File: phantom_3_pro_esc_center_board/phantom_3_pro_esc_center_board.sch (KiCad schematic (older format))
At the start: 0 parts

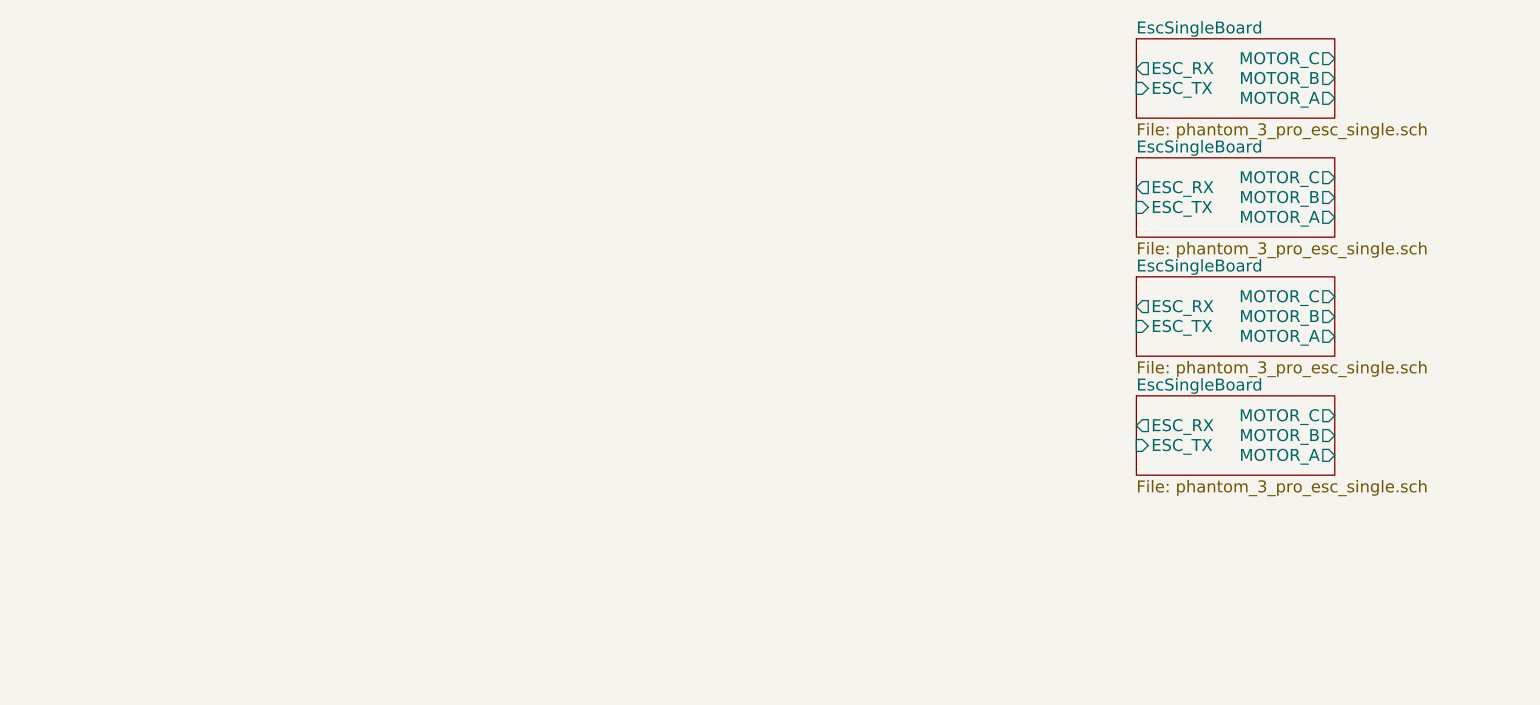
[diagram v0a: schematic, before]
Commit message: Renumbered components.
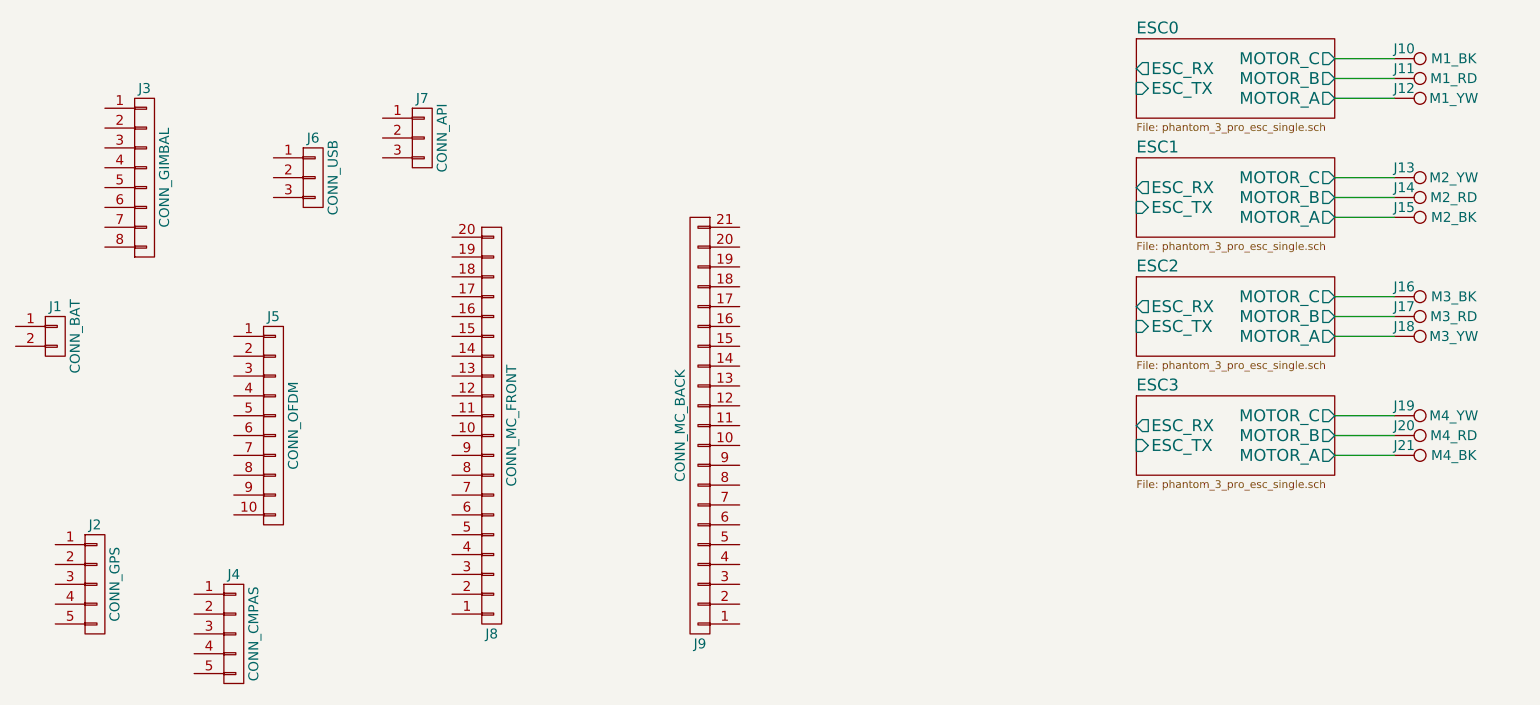
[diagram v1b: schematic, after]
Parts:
- added J1: CONN_BAT, symbol CONN_01X02
- added J10: M1_BK, symbol TEST_1P
- added J11: M1_RD, symbol TEST_1P
- added J12: M1_YW, symbol TEST_1P
- added J13: M2_YW, symbol TEST_1P
- added J14: M2_RD, symbol TEST_1P
- added J15: M2_BK, symbol TEST_1P
- added J16: M3_BK, symbol TEST_1P
- added J17: M3_RD, symbol TEST_1P
- added J18: M3_YW, symbol TEST_1P
- added J19: M4_YW, symbol TEST_1P
- added J2: CONN_GPS, symbol CONN_01X05
- added J20: M4_RD, symbol TEST_1P
- added J21: M4_BK, symbol TEST_1P
- added J3: CONN_GIMBAL, symbol CONN_01X08
- added J4: CONN_CMPAS, symbol CONN_01X05
- added J5: CONN_OFDM, symbol CONN_01X10
- added J6: CONN_USB, symbol CONN_01X03
- added J7: CONN_API, symbol CONN_01X03
- added J8: CONN_MC_FRONT, symbol CONN_01X20
- added J9: CONN_MC_BACK, symbol CONN_01X21
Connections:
- new net ESC0/MOTOR_A: J12.1
- new net ESC0/MOTOR_B: J11.1
- new net ESC0/MOTOR_C: J10.1
- new net ESC1/MOTOR_A: J15.1
- new net ESC1/MOTOR_B: J14.1
- new net ESC1/MOTOR_C: J13.1
- new net ESC2/MOTOR_A: J18.1
- new net ESC2/MOTOR_B: J17.1
- new net ESC2/MOTOR_C: J16.1
- new net ESC3/MOTOR_A: J21.1
- new net ESC3/MOTOR_B: J20.1
- new net ESC3/MOTOR_C: J19.1

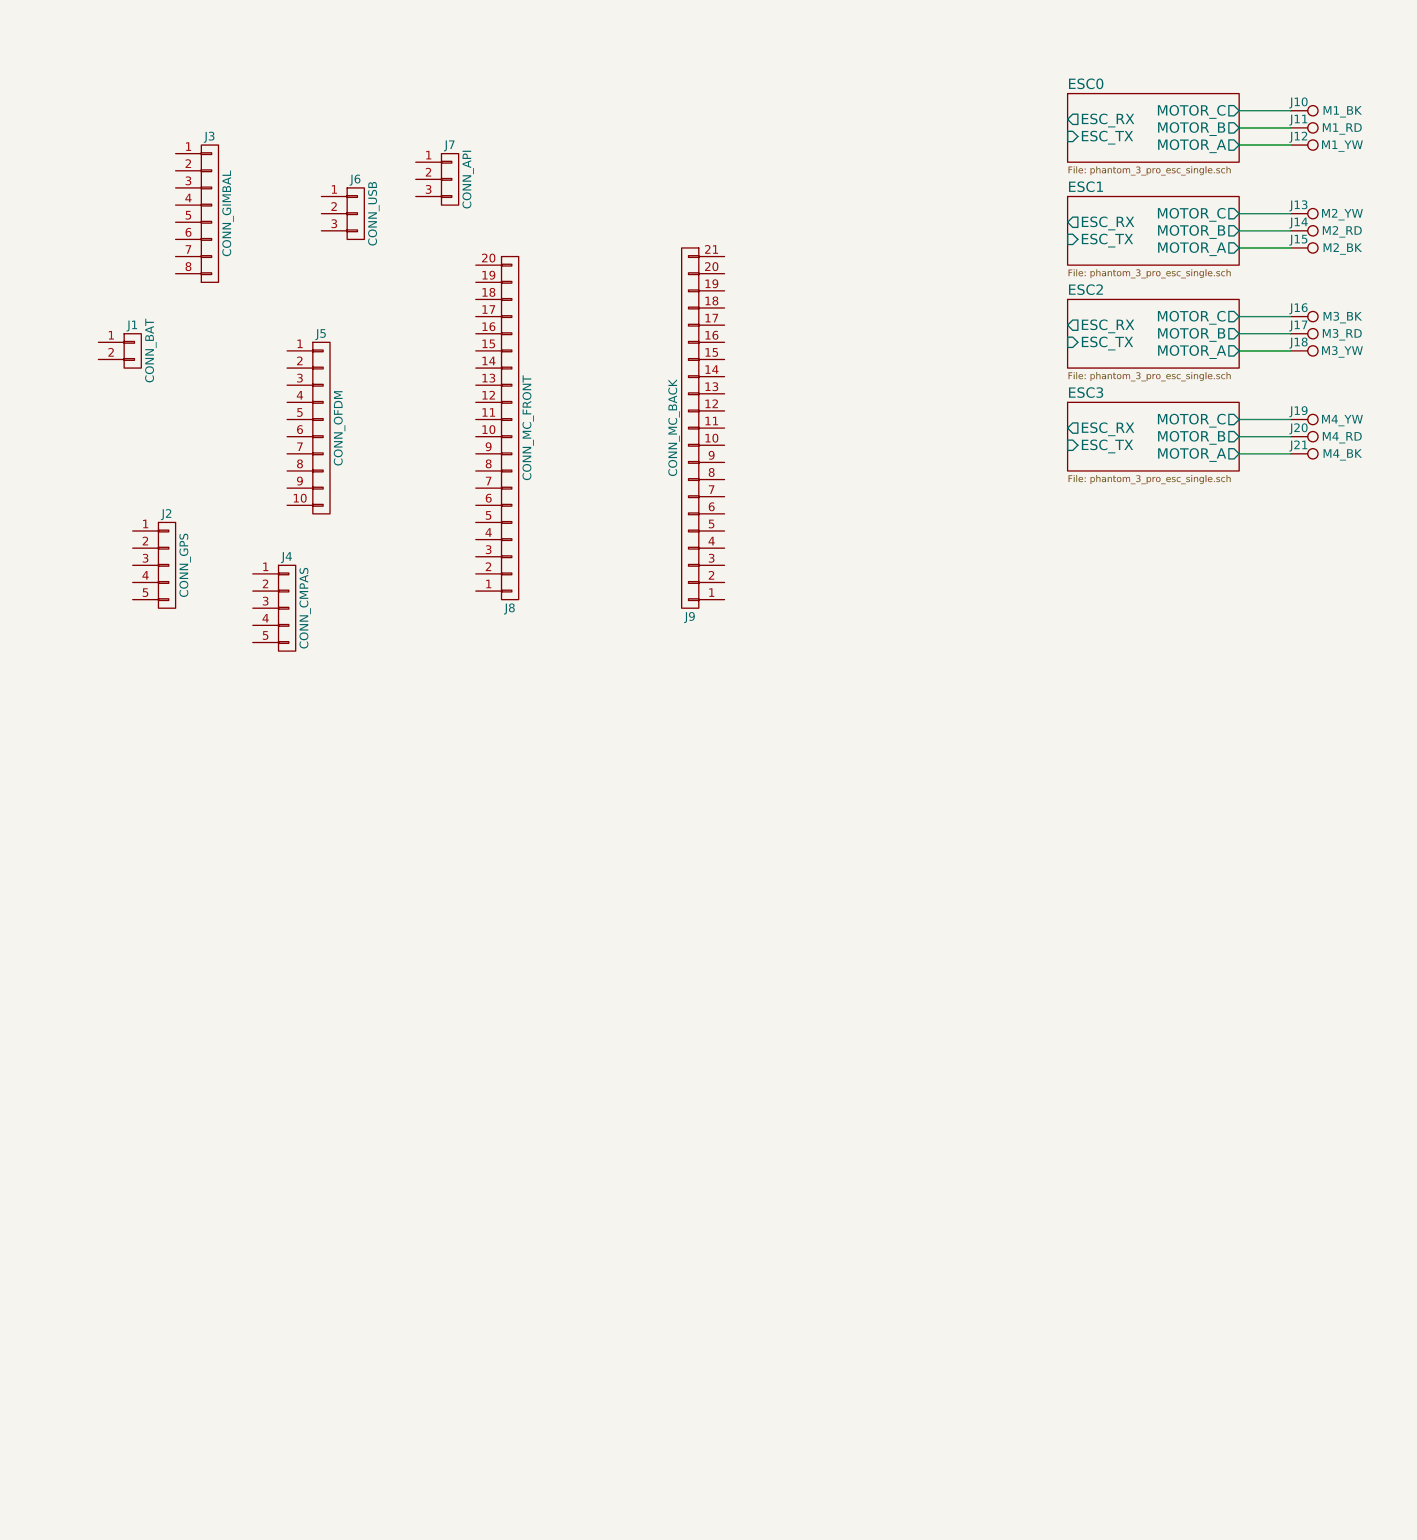
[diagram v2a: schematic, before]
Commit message: ESC Center: Identified pins of FC connection.
Named all FC pins, and linked with proper connectors.
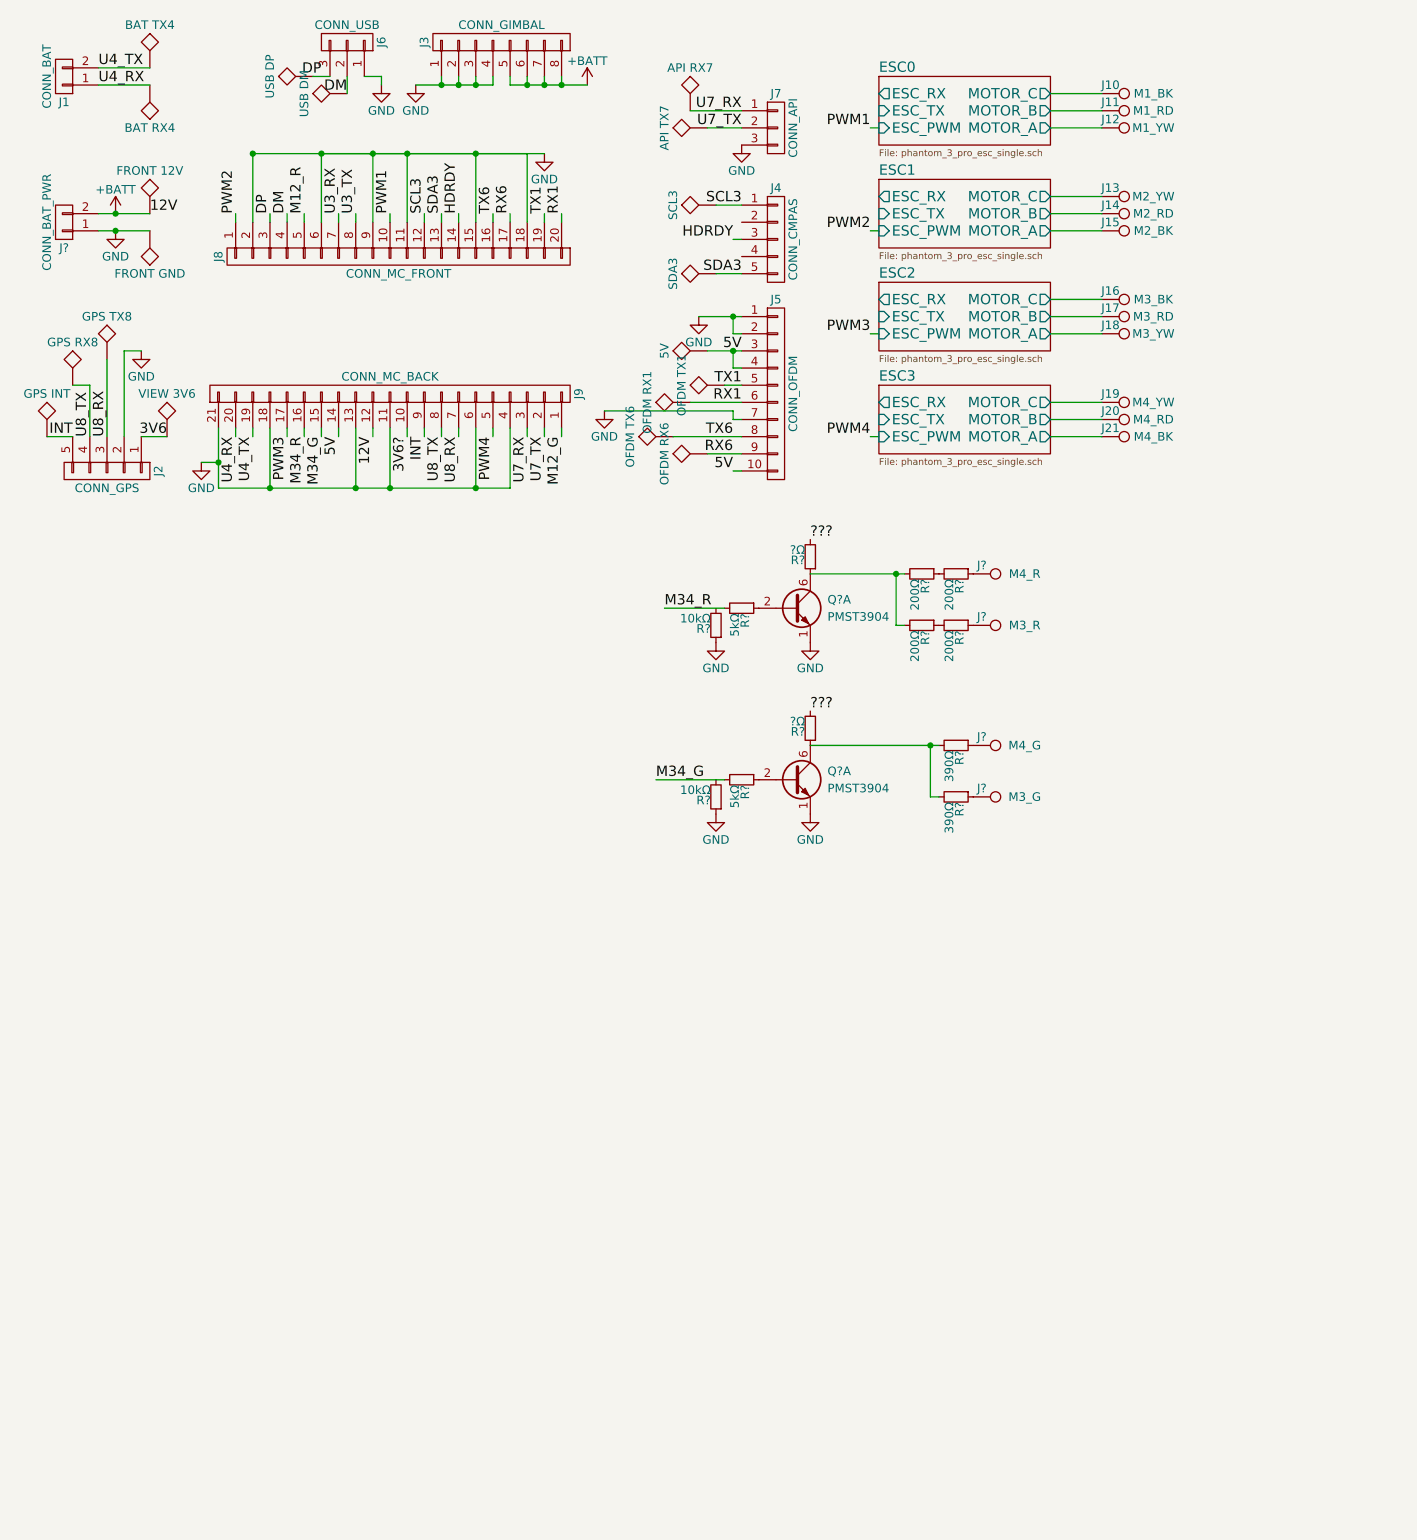
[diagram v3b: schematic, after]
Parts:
- added J?: CONN_BAT_PWR, symbol CONN_01X02
- added J?: M4_R, symbol TEST_1P
- added J?: M4_G, symbol TEST_1P
- added J?: M3_R, symbol TEST_1P
- added J?: M3_G, symbol TEST_1P
- added Q? (x2): PMST3904, TO_SOT_Packages_SMD:SOT-363, symbol PMBT2222AYS
- added R? (x4): 200Ω, symbol R_Small
- added R? (x2): 390Ω, symbol R_Small
- added R? (x2): 5kΩ, symbol R_Small
- added R? (x2): 10kΩ, symbol R_Small
- added R? (x2): ?Ω, symbol R_Small
- added TP?: GPS INT, symbol TEST
- added TP?: OFDM TX6, symbol TEST
- added TP?: GPS TX8, symbol TEST
- added TP?: FRONT 12V, symbol TEST
- added TP?: FRONT GND, symbol TEST
- added TP?: BAT TX4, symbol TEST
- added TP?: BAT RX4, symbol TEST
- added TP?: VIEW 3V6, symbol TEST
- added TP?: USB DP, symbol TEST
- added TP?: USB DM, symbol TEST
- added TP?: API RX7, symbol TEST
- added TP?: OFDM RX1, symbol TEST
- added TP?: API TX7, symbol TEST
- added TP?: 5V, symbol TEST
- added TP?: OFDM RX6, symbol TEST
- added TP?: SCL3, symbol TEST
- added TP?: SDA3, symbol TEST
- added TP?: OFDM TX1, symbol TEST
- added TP?: GPS RX8, symbol TEST
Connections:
- net PWM2: now reaches J8.1 (P1)
- net PWM1: now reaches J8.10 (P10)
- net GND: now reaches J8.11 (P11)
- net GND: now also J2.2 (P2), J3.1 (P1), J3.2 (P2), J3.3 (P3), J3.4 (P4), J5.1 (P1), J5.2 (P2), J5.7 (P7), J6.1 (P1), J7.3 (P3), J8.15 (P15), J8.18 (P18), J8.2 (P2), J8.6 (P6), J8.9 (P9), J9.11 (P11), J9.13 (P13), J9.18 (P18), J9.21 (P21), J9.4 (P4), J9.6 (P6), J?.1 (P1), Q?.1 (E1), Q?.1 (E1), R?.1, R?.1, TP?.1
- net SCL3: now reaches J8.12 (P12)
- net SCL3: now also J4.1 (P1), TP?.1
- net SDA3: now reaches J8.13 (P13)
- net SDA3: now also J4.5 (P5), TP?.1
- net HDRDY: now reaches J8.14 (P14)
- net HDRDY: now also J4.3 (P3)
- net TX6: now reaches J8.16 (P16)
- net TX6: now also J5.8 (P8), TP?.1
- net RX6: now reaches J8.17 (P17)
- net RX6: now also J5.9 (P9), TP?.1
- net TX1: now reaches J8.19 (P19)
- net TX1: now also J5.5 (P5), TP?.1
- net RX1: now reaches J8.20 (P20)
- net RX1: now also J5.6 (P6), TP?.1
- net DP: now reaches J8.3 (P3)
- net DP: now also J6.3 (P3), TP?.1
- net DM: now reaches J8.4 (P4)
- net DM: now also J6.2 (P2), TP?.1
- net M12_R: now reaches J8.5 (P5)
- net U3_RX: now reaches J8.7 (P7)
- net U3_TX: now reaches J8.8 (P8)
- net M12_G: now reaches J9.1 (P1)
- net 3V6?: now reaches J9.10 (P10)
- net +BATT: now reaches J9.12 (P12)
- net +BATT: now also J3.5 (P5), J3.6 (P6), J3.7 (P7), J3.8 (P8), J?.2 (P2), TP?.1
- net 5V: now reaches J9.14 (P14)
- net 5V: now also J5.10 (P10), J5.3 (P3), J5.4 (P4), TP?.1
- net M34_G: now reaches J9.15 (P15)
- net M34_G: now also R?.2
- net M34_R: now reaches J9.16 (P16)
- net M34_R: now also R?.2
- net PWM3: now reaches J9.17 (P17)
- net U4_TX: now reaches J9.19 (P19)
- net U4_TX: now also J1.2 (P2), TP?.1
- net U7_TX: now reaches J9.2 (P2)
- net U7_TX: now also J7.2 (P2), TP?.1
- net U4_RX: now reaches J9.20 (P20)
- net U4_RX: now also J1.1 (P1), TP?.1
- net U7_RX: now reaches J9.3 (P3)
- net U7_RX: now also J7.1 (P1), TP?.1
- net PWM4: now reaches J9.5 (P5)
- net U8_RX: now reaches J9.7 (P7)
- net U8_RX: now also J2.3 (P3), TP?.1
- net U8_TX: now reaches J9.8 (P8)
- net U8_TX: now also J2.4 (P4), TP?.1
- net INT: now reaches J9.9 (P9)
- net INT: now also J2.5 (P5), TP?.1
- net 3V6: now reaches J2.1 (P1)
- net 3V6: now also TP?.1
- new net: R?.1, R?.2 (x2)
- new net: Q?.6 (C1), R?.1, R?.2, R?.2 (x2)
- new net: J?.1, R?.1 (x4)
- new net: Q?.2 (B1), R?.1 (x2)
- new net ???: R?.2, R?.2
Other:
- moved on the sheet: J1, J10, J11, J12, J13, J14, J15, J16, J17, J18, J19, J2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
